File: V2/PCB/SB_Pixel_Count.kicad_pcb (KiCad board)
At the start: 2 copper layers, 53.5 x 26.5 mm, 20 parts, among them J2 String1, J3 OLED, SW1 Test, SW2 Test, U1 74AHCT1G125, U2 MOUDLE-SEEEDUINO-XIAO, U3 AMS1117-5.0, U4 INA219BxD, U5 TF-123-ARP9H17

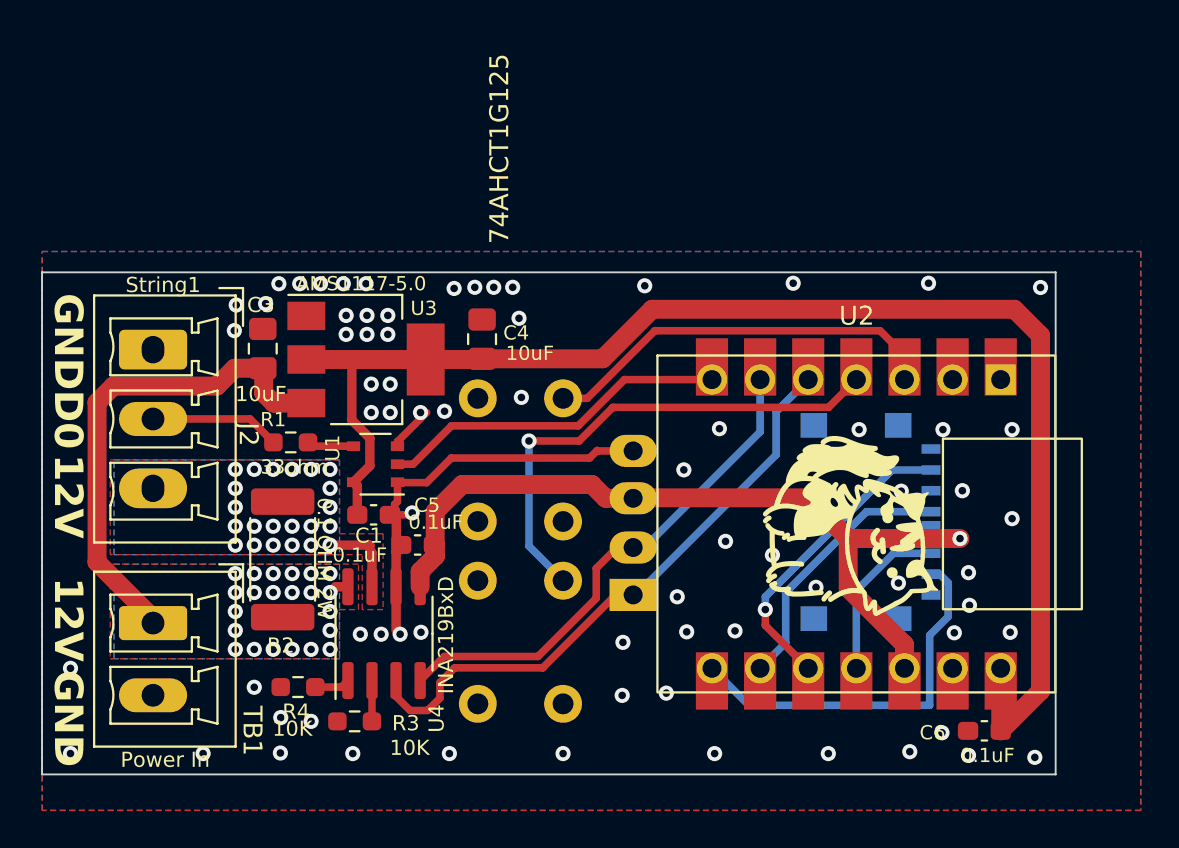
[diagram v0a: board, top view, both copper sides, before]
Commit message: Rename RP2040_Count files/folders to SB_Pixel_Count across all variants
Renames the KiCad project quads (.kicad_pcb/.kicad_sch/.kicad_pro/.kicad_prl),
exported BOM/gerber/production files, case STL/FCStd files, and the
Firmware/RP2040_Count sketch (-> Firmware/SB_Pixel_Count, matching the
required folder/.ino name convention) in V1, V2, V2 Lite, and V3 Pro.

Fixes up internal cross-references that would otherwise go stale:
- kicad_pcb sheetfile metadata and kicad_sch symbol instance "project" fields
- kicad_pro/kicad_prl self-referencing "filename" fields and bom_export_filename
- .github/workflows/compile.yml and drc.yml sketch/DRC paths
- README.md links and ATtiny1614_Count.ino header comments

Verified the renamed Firmware/SB_Pixel_Count sketch still compiles
(VERSION2/seeed_xiao_rp2040) after the rename.

Co-Authored-By: Claude Sonnet 5 <noreply@anthropic.com>
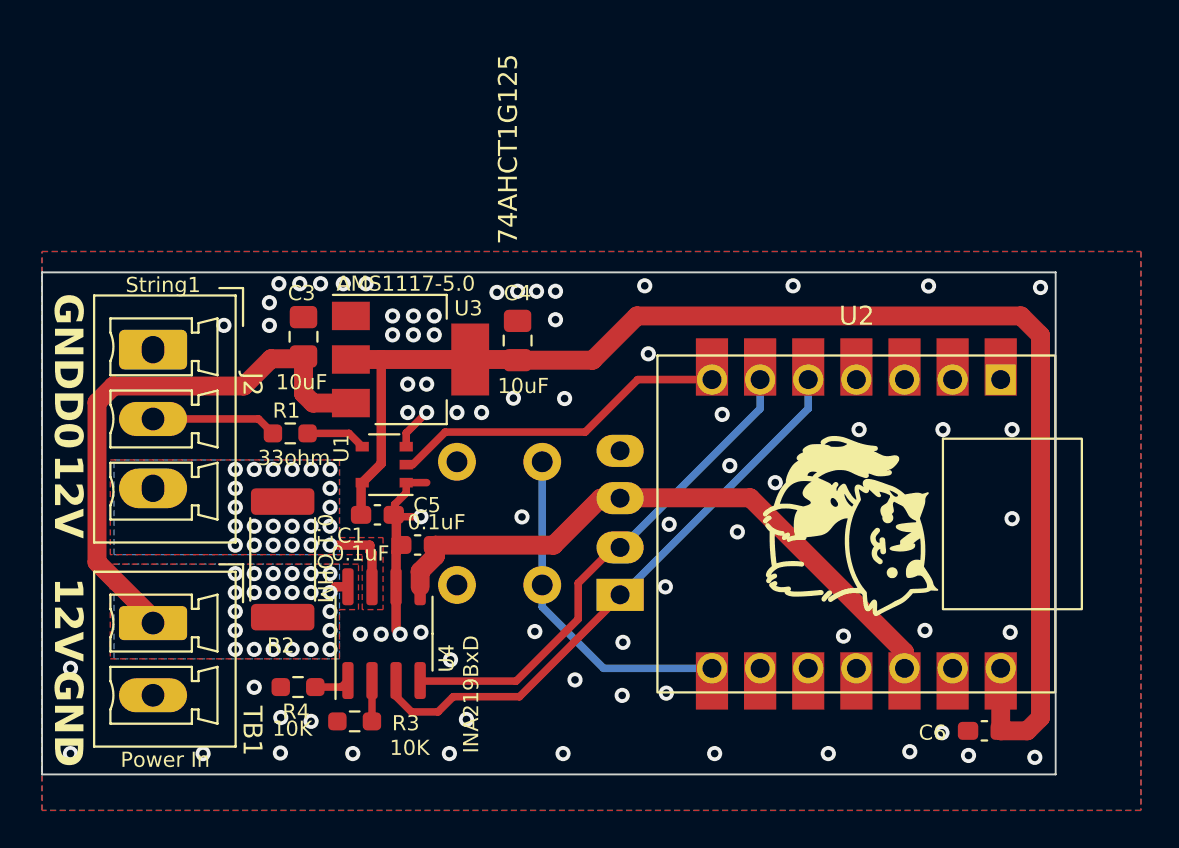
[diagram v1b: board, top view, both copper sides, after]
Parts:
- removed SW2: Test, Button_Switch_THT:SW_PUSH_6mm
- removed U5: TF-123-ARP9H17, TF-SMD_TF:TF-SMD_TF-123-ARP9H15
- R2: value 0.1 OHM 2W -> 0.1 OHM
- moved SW1 3.53 mm to (125.9, 90.1)
- moved U3 2.35 mm to (119.0, 78.2)
- moved C3 2.24 mm to (113.3, 77.0)
- moved C4 1.88 mm to (124.6, 77.2)
- moved J3 0.69 mm to (130.0, 86.8)
- moved R1 0.48 mm to (112.6, 82.1)
- moved U1 0.46 mm to (117.6, 83.8)
- moved C1 0.20 mm to (117.2, 86.4)
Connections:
- U2 pad 10: DO -> unconnected-(U2-PA5_A9_D9_MISO-Pad10)
- U2 pad 11: DI -> unconnected-(U2-PA6_A10_D10_MOSI-Pad11)
- U2 pad 3: SW1 -> unconnected-(U2-PA10_A2_D2-Pad3)
- U2 pad 4: SW2 -> unconnected-(U2-PA11_A3_D3-Pad4)
- U2 pad 8: CS -> SW1
- U2 pad 9: CLK -> unconnected-(U2-PA7_A8_D8_SCK-Pad9)
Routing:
- net SW2: track 26.7 -> 0.00 mm, vias 1 -> 0
- net CS: track 20.3 -> 0.00 mm
- net DO: track 16.2 -> 0.00 mm, vias 1 -> 0
- net CLK: track 14.0 -> 0.00 mm
- net GND: track 25.6 -> 13.5 mm
- net +3.3V: track 43.4 -> 32.6 mm, vias 1 -> 0
- net DI: track 8.86 -> 0.00 mm
- net SW1: track 21.6 -> 18.0 mm
- net VIN1: track 27.7 -> 30.5 mm
- net +5V: track 74.1 -> 72.3 mm
- net I2C_SDA: track 32.0 -> 31.1 mm
- net Net-(R1-Pad2): track 2.49 -> 3.18 mm
- net I2C_SCL: track 27.1 -> 26.6 mm
